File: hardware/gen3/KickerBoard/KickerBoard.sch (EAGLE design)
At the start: 109 parts, among them U2 ATMEGA165PV-8AU

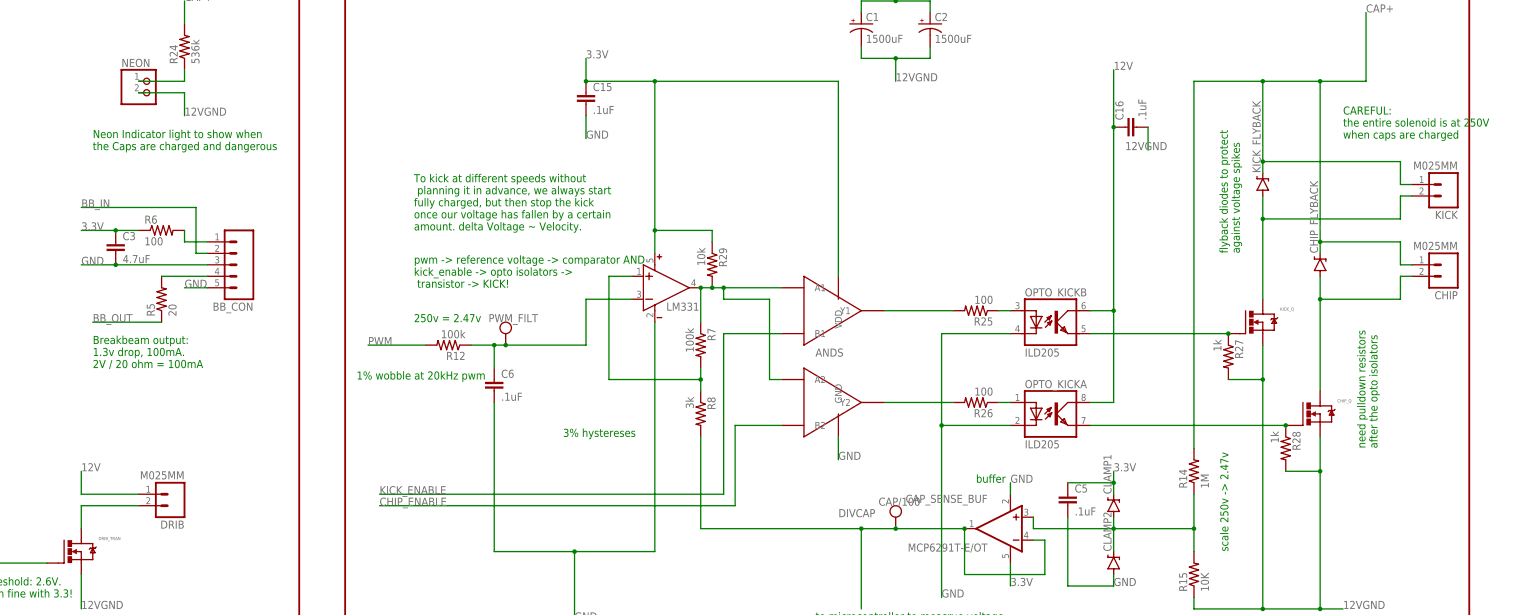
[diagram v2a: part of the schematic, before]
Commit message: finished parts for kicker. damn picking connectors is annoying
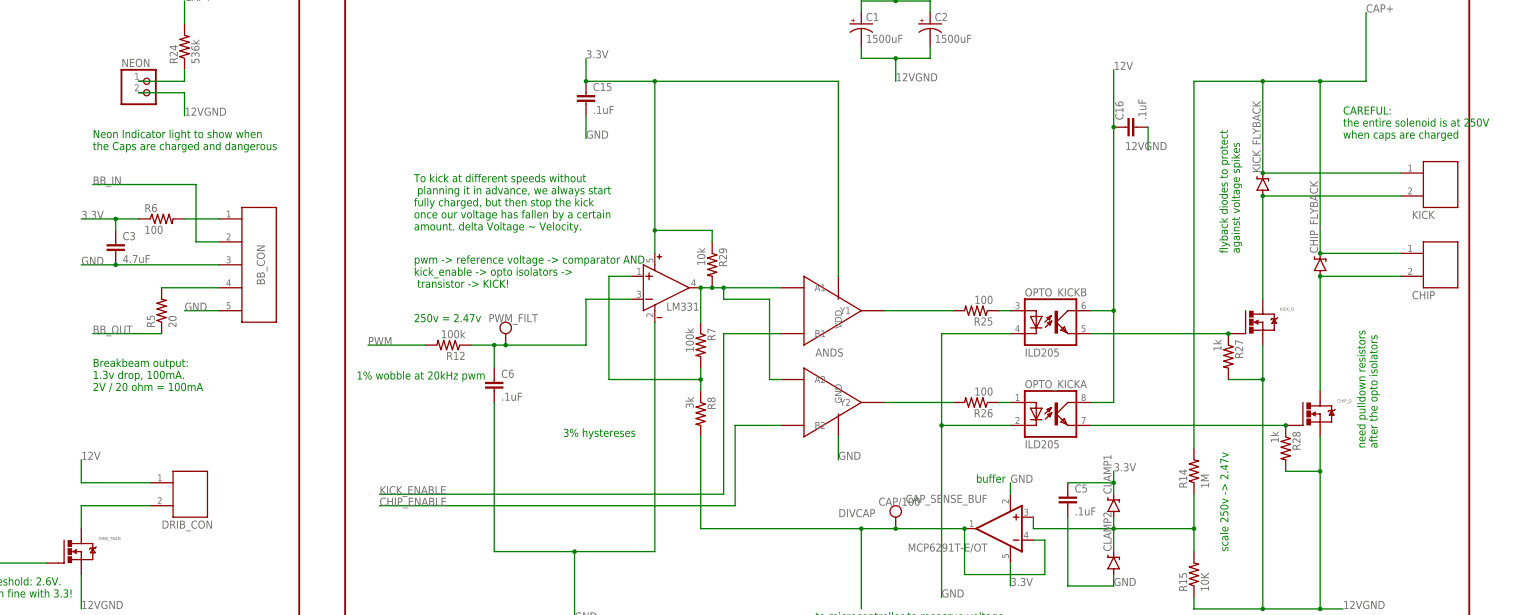
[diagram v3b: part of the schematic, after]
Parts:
- removed DRIB: M025MM, SparkFun-Connectors:M025MM
- removed TRANSFORMER: 32052-TRANSFORMER, kickerchips:32052-TRANSFORMER
- added DRIB_CON: JST-22MM, gen3:JST-22MM
- added U$1: 32052-TRANSFORMER, gen3:32052-TRANSFORMER
- BB_CON: value (none) -> JST-5; device SparkFun-Connectors:M05LOCK -> gen3:JST-5
- CHIP, KICK: value M025MM -> JST-22MM; device SparkFun-Connectors:M025MM -> gen3:JST-22MM
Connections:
- net 12V: now also U$1.P$4, U$1.P$5; no longer DRIB.1, TRANSFORMER.P$4, TRANSFORMER.P$5
- net 12VGND: now also U$1.P$10; no longer TRANSFORMER.P$10
- net BB_IN: now also BB_CON.P$2; no longer BB_CON.2
- net CAP+: now also CHIP.P$1, KICK.P$1; no longer CHIP.1, KICK.1
- net GND: now also BB_CON.P$3, BB_CON.P$5; no longer BB_CON.3, BB_CON.5
- net N$32: now also BB_CON.P$4; no longer BB_CON.4
- net N$33: now also KICK.P$2; no longer KICK.2
- net N$34: now also CHIP.P$2; no longer CHIP.2
- net N$40: now also BB_CON.P$1; no longer BB_CON.1
- net N$5: now also U$1.P$6, U$1.P$7; no longer TRANSFORMER.P$6, TRANSFORMER.P$7
- net TO_DRIB: no longer DRIB.2
- net TRANS_OUT: now also U$1.P$1; no longer TRANSFORMER.P$1
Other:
- moved on the sheet: R5, R6

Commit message: cleared some kicker
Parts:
- GEN_3_REV_B: value LOGO -> Spring 2015
- renumbered U$9 to GEN_3_REV_B
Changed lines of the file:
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@@
 <part name="C22" library="SparkFun-Capacitors" deviceset="CAP" device="0805" value=".01uF"/>
 <part name="5.0REG" library="SparkFun-PowerIC" deviceset="V_REG_MIC5219" device="5V" value="MIC5219 5V"/>
-<part name="U$9" library="gen3" deviceset="LOGO" device=""/>
+<part name="GEN_3_REV_B" library="gen3" deviceset="LOGO" device="" value="Spring 2015"/>
 <part name="C23" library="SparkFun-Capacitors" deviceset="CAP" device="1206" value="47uF"/>
 <part name="SWITCH_Q" library="gen3" deviceset="N-MOSFET" device="DPAK"/>
@@
 <instance part="C22" gate="G$1" x="104.14" y="165.1" rot="R90"/>
 <instance part="5.0REG" gate="G$1" x="68.58" y="322.58"/>
-<instance part="U$9" gate="G$1" x="30.48" y="99.06"/>
+<instance part="GEN_3_REV_B" gate="G$1" x="30.48" y="99.06"/>
 <instance part="C23" gate="G$1" x="421.64" y="63.5"/>
 <instance part="SWITCH_Q" gate="G$1" x="381" y="101.6"/>

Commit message: work on kicker
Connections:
- net 12V: now also DRIB_CON.P$1
- net TO_DRIB: now also DRIB_CON.P$2
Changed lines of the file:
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@@
 <wire x1="200.66" y1="264.16" x2="215.9" y2="264.16" width="0.1524" layer="91"/>
 <label x="200.66" y="269.24" size="1.778" layer="95"/>
+<pinref part="DRIB_CON" gate="G$1" pin="P$1"/>
 </segment>
 <segment>
@@
 <wire x1="200.66" y1="259.08" x2="200.66" y2="254" width="0.1524" layer="91"/>
 <pinref part="DRIB_TRAN" gate="G$1" pin="D"/>
-</segment>
-</net>
+<pinref part="DRIB_CON" gate="G$1" pin="P$2"/>
+</segment>
+</net>

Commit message: almost done with power for kicker
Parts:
- C10, C11: value 100uF -> 47uF; device gen3:CAP-POLAR -> SparkFun-Capacitors:CAP1206
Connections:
- net 3.3V: now also C10.1; no longer C10.+
- net 5V: now also C11.1; no longer C11.+
- net GND: now also C10.2, C11.2; no longer C10.-, C11.-
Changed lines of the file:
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@@
 <part name="DIS" library="gen3" deviceset="TEST_PT" device=""/>
 <part name="C8" library="SparkFun-Capacitors" deviceset="CAP" device="0805" value="470pF"/>
-<part name="C10" library="gen3" deviceset="CAP-POLAR" device="" value="100uF"/>
-<part name="C11" library="gen3" deviceset="CAP-POLAR" device="" value="100uF"/>
 <part name="R11" library="SparkFun-Passives" deviceset="RESISTOR" device="0805-RES" value="100k"/>
 <part name="R31" library="SparkFun-Passives" deviceset="RESISTOR" device="0805-RES" value="43k"/>
@@
 <part name="DRIB_CON" library="gen3" deviceset="JST-2" device="2MM"/>
 <part name="U$1" library="gen3" deviceset="32052-TRANSFORMER" device=""/>
+<part name="C10" library="SparkFun-Capacitors" deviceset="CAP" device="1206" value="47uF"/>
+<part name="C11" library="SparkFun-Capacitors" deviceset="CAP" device="1206" value="47uF"/>
 </parts>
 <sheets>
@@
 <instance part="DIS" gate="G$1" x="469.9" y="78.74"/>
 <instance part="C8" gate="G$1" x="78.74" y="312.42"/>
-<instance part="C10" gate="G$1" x="86.36" y="353.06"/>
-<instance part="C11" gate="G$1" x="86.36" y="312.42"/>
 <instance part="R11" gate="G$1" x="294.64" y="124.46" rot="R90"/>
 <instance part="R31" gate="G$1" x="363.22" y="104.14"/>
@@
 <instance part="DRIB_CON" gate="G$1" x="220.98" y="261.62"/>
 <instance part="U$1" gate="G$1" x="421.64" y="124.46"/>
+<instance part="C10" gate="G$1" x="86.36" y="350.52"/>
+<instance part="C11" gate="G$1" x="86.36" y="309.88"/>
 </instances>
 <busses>
@@
 <wire x1="99.06" y1="347.98" x2="99.06" y2="345.44" width="0.1524" layer="91"/>
 <wire x1="99.06" y1="345.44" x2="86.36" y2="345.44" width="0.1524" layer="91"/>
-<pinref part="C10" gate="G$1" pin="-"/>
 <pinref part="C7" gate="G$1" pin="2"/>
 <wire x1="111.76" y1="347.98" x2="111.76" y2="345.44" width="0.1524" layer="91"/>
@@
 <junction x="99.06" y="345.44"/>
 <wire x1="99.06" y1="345.44" x2="99.06" y2="342.9" width="0.1524" layer="91"/>
+<pinref part="C10" gate="G$1" pin="2"/>
 </segment>
 <segment>
@@
 <wire x1="99.06" y1="307.34" x2="99.06" y2="304.8" width="0.1524" layer="91"/>
 <wire x1="99.06" y1="304.8" x2="86.36" y2="304.8" width="0.1524" layer="91"/>
-<pinref part="C11" gate="G$1" pin="-"/>
 <junction x="86.36" y="304.8"/>
 <wire x1="53.34" y1="304.8" x2="78.74" y2="304.8" width="0.1524" layer="91"/>
@@
 <wire x1="58.42" y1="322.58" x2="53.34" y2="322.58" width="0.1524" layer="91"/>
 <junction x="53.34" y="322.58"/>
+<pinref part="C11" gate="G$1" pin="2"/>
 </segment>
 <segment>
@@
 <wire x1="99.06" y1="358.14" x2="91.44" y2="358.14" width="0.1524" layer="91"/>
 <junction x="99.06" y="358.14"/>
-<pinref part="C10" gate="G$1" pin="+"/>
 <wire x1="86.36" y1="355.6" x2="86.36" y2="358.14" width="0.1524" layer="91"/>
 <wire x1="91.44" y1="358.14" x2="86.36" y2="358.14" width="0.1524" layer="91"/>
@@
 <wire x1="73.66" y1="358.14" x2="86.36" y2="358.14" width="0.1524" layer="91"/>
 <junction x="86.36" y="358.14"/>
+<pinref part="C10" gate="G$1" pin="1"/>
 </segment>
 <segment>
@@
 </segment>
 <segment>
-<pinref part="C11" gate="G$1" pin="+"/>
 <wire x1="86.36" y1="317.5" x2="86.36" y2="314.96" width="0.1524" layer="91"/>
 <wire x1="111.76" y1="317.5" x2="116.84" y2="317.5" width="0.1524" layer="91"/>
@@
 <wire x1="76.2" y1="327.66" x2="86.36" y2="327.66" width="0.1524" layer="91"/>
 <wire x1="86.36" y1="327.66" x2="86.36" y2="317.5" width="0.1524" layer="91"/>
-</segment>
-</net>
+<pinref part="C11" gate="G$1" pin="1"/>
+</segment>
+</net>

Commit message: finished kicker board!
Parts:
- renumbered DRIB_CON to DRIB
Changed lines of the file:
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@@
 <part name="CHIP" library="gen3" deviceset="JST-2" device="2MM"/>
 <part name="BB_CON" library="gen3" deviceset="JST-5" device=""/>
-<part name="DRIB_CON" library="gen3" deviceset="JST-2" device="2MM"/>
+<part name="DRIB" library="gen3" deviceset="JST-2" device="2MM"/>
 <part name="U$1" library="gen3" deviceset="32052-TRANSFORMER" device=""/>
 <part name="C10" library="SparkFun-Capacitors" deviceset="CAP" device="1206" value="47uF"/>
@@
 <instance part="CHIP" gate="G$1" x="497.84" y="312.42"/>
 <instance part="BB_CON" gate="G$1" x="238.76" y="312.42"/>
-<instance part="DRIB_CON" gate="G$1" x="220.98" y="261.62"/>
+<instance part="DRIB" gate="G$1" x="220.98" y="261.62"/>
 <instance part="U$1" gate="G$1" x="421.64" y="124.46"/>
 <instance part="C10" gate="G$1" x="86.36" y="350.52"/>
@@
 <wire x1="200.66" y1="264.16" x2="215.9" y2="264.16" width="0.1524" layer="91"/>
 <label x="200.66" y="269.24" size="1.778" layer="95"/>
-<pinref part="DRIB_CON" gate="G$1" pin="P$1"/>
+<pinref part="DRIB" gate="G$1" pin="P$1"/>
 </segment>
 <segment>
@@
 <wire x1="200.66" y1="259.08" x2="200.66" y2="254" width="0.1524" layer="91"/>
 <pinref part="DRIB_TRAN" gate="G$1" pin="D"/>
-<pinref part="DRIB_CON" gate="G$1" pin="P$2"/>
-</segment>
-</net>
+<pinref part="DRIB" gate="G$1" pin="P$2"/>
+</segment>
+</net>

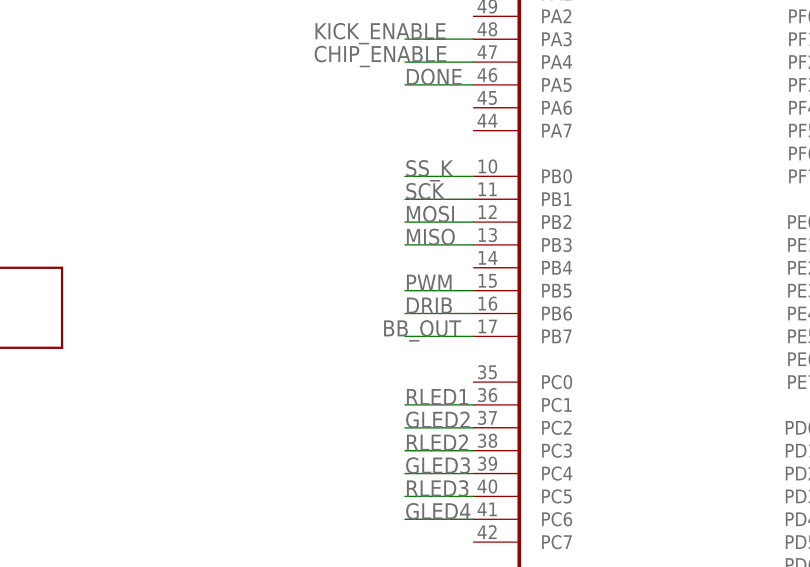
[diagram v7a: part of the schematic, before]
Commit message: weird linking errors after adding more defines
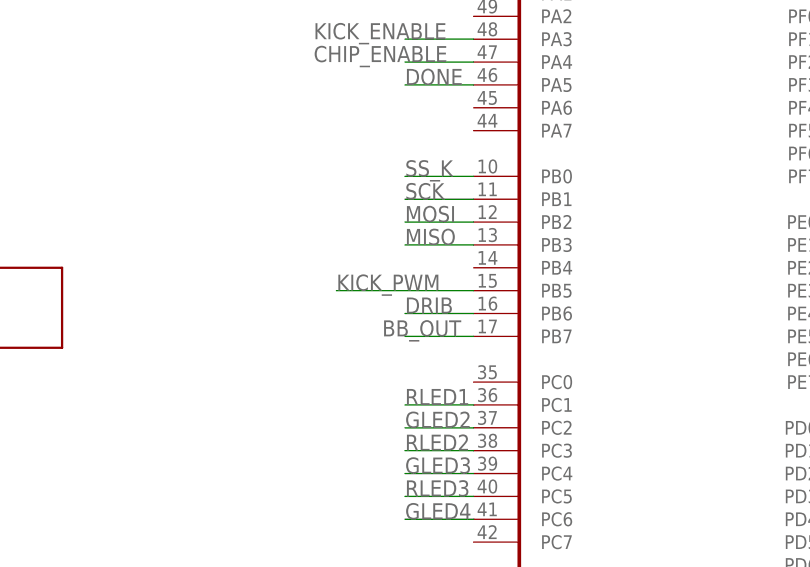
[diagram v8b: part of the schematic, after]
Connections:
- new net KICK_PWM: U2.PB5
- net PWM: no longer U2.PB5
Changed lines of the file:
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@@
 <?xml version="1.0" encoding="utf-8"?>
 <!DOCTYPE eagle SYSTEM "eagle.dtd">
-<eagle version="6.4">
+<eagle version="7.2.0">
 <drawing>
 <settings>
@@
 <label x="264.16" y="294.64" size="1.778" layer="95"/>
 </segment>
-<segment>
-<pinref part="U2" gate="A" pin="PB5"/>
-<wire x1="101.6" y1="104.14" x2="93.98" y2="104.14" width="0.1524" layer="91"/>
-<label x="93.98" y="104.14" size="1.778" layer="95"/>
-</segment>
 </net>
 <net name="N$13" class="0">
@@
 </segment>
 </net>
+<net name="KICK_PWM" class="0">
+<segment>
+<pinref part="U2" gate="A" pin="PB5"/>
+<wire x1="101.6" y1="104.14" x2="86.36" y2="104.14" width="0.1524" layer="91"/>
+<label x="86.36" y="104.14" size="1.778" layer="95"/>
+</segment>
+</net>
